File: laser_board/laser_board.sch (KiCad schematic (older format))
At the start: 14 parts

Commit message: Adding some goodies to the laser board: 1. Laser driver 2. AVR programmer 3. Fixing a wrong wiring (arduino pin #2) 4. Crystal oscillator 5. Reset pin
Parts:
- removed UL?: JohnsLaserDriver, symbol JohnsLaserDriver
- added C?: 100nF, symbol C
- added C? (x2): 22pF, symbol C
- added D? (x2): D, symbol D
- added LAIZAA: CONN_01X02, symbol CONN_01X02
- added PROG: CONN_02X03, symbol CONN_02X03
- added Q?: Q_NPN_EBC, symbol Q_NPN_EBC
- added R?: 10K, symbol R
- added R?: 1R0, symbol R
- added R?: 180R, symbol R
- added RV?: POT, symbol POT
- added U?: LM317T, TO-220, symbol LM317T
- added Y?: Crystal, symbol Crystal
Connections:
- wire segments 100 -> 171
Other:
- moved on the sheet: IC?

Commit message: Schematics changes: 1. Adding UART 2. Adding a power connector 3. Adding some footprints 4. Adding a reset button 5. Adding some decoupling capacitors
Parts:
- removed SW_MS1, SW_MS2, SW_MS3: SPST, symbol SPST
- added C?: 100nF, symbol C
- added C? (x3): 47uF, symbol CP
- added MICROSTEP: CONN_02X03, Pin_Headers:Pin_Header_Straight_2x03, symbol CONN_02X03
- added POWER: CONN_01X03, Sockets_MOLEX_KK-System:Socket_MOLEX-KK-RM2-54mm_Lock_3pin_straight, symbol CONN_01X03
- added R? (x2): 1K, symbol R
- added SW?: SW_PUSH, symbol SW_PUSH
- added UART: CONN_01X03, Pin_Headers:Pin_Header_Straight_1x03, symbol CONN_01X03
- LAIZAA, PSX, PSY: footprint (none) -> Sockets_MOLEX_KK-System:Socket_MOLEX-KK-RM2-54mm_Lock_2pin_straight
- PROG: footprint (none) -> Pin_Headers:Pin_Header_Straight_2x03
- PX1, PX2, PY: footprint (none) -> Sockets_MOLEX_KK-System:Socket_MOLEX-KK-RM2-54mm_Lock_4pin_straight
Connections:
- wire segments 171 -> 195
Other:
- moved on the sheet: D?, LAIZAA, R?, RV?, U?

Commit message: Adding a footprint for the A4988 board Assigning footprints Adding a PCB
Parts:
- removed C?: 100nF, symbol C
- removed Q?: Q_NPN_EBC, symbol Q_NPN_EBC
- added C4: 10uF, Capacitors_ThroughHole:C_Radial_D5_L11_P2.5, symbol CP
- added Q1: IRF540N, Power_Integrations:TO-220, symbol IRF540N
- added R6: 1R0, Resistors_ThroughHole:Resistor_Vertical_RM5mm, symbol R
- C1, C2, C3: renamed from C?; footprint (none) -> Capacitors_ThroughHole:C_Rect_L4_W2.5_P2.5
- C5, C6, C7: renamed from C?; footprint (none) -> Capacitors_ThroughHole:C_Radial_D6.3_L11.2_P2.5
- D1, D2: renamed from D?; footprint (none) -> Diodes_ThroughHole:Diode_DO-41_SOD81_Vertical_KathodeUp
- IC1: renamed from IC?; footprint DIL28 -> Housings_DIP:DIP-28_W7.62mm
- POWER1: renamed from POWER; symbol CONN_01X03 -> CONN_01X03-RESCUE-laser_board
- R1: value R -> 220R; footprint (none) -> Capacitors_ThroughHole:C_Rect_L4_W2.5_P2.5
- R2, R3, R4, R7: renamed from R?; footprint (none) -> Capacitors_ThroughHole:C_Rect_L4_W2.5_P2.5
- R5: renamed from R?; footprint (none) -> Resistors_ThroughHole:Resistor_Vertical_RM5mm
- RV1: renamed from RV?; footprint (none) -> Potentiometers:Potentiometer_Bourns_3006P_Angular_ScrewFront
- SW1: renamed from SW?; footprint (none) -> Pin_Headers:Pin_Header_Straight_1x02
- U1: renamed from U?; footprint TO-220 -> Power_Integrations:TO-220
- UART1: renamed from UART; symbol CONN_01X03 -> CONN_01X03-RESCUE-laser_board
- UX1, UX2: footprint (none) -> My_Shit:A4988
- UY1: renamed from UY; footprint (none) -> My_Shit:A4988
- Y1: renamed from Y?; footprint (none) -> Crystals:Crystal_HC49-U_Vertical
- renumbered LAIZAA to LAIZAA1, MICROSTEP to MICROSTEP1, PROG to PROG1, PSX to PSX1, PSY to PSY1, PY to PY1
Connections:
- wire segments 195 -> 158
- no-connect marks 0 -> 10
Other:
- moved on the sheet: R5, R7

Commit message: major PCB improvements
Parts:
- RV1: symbol POT -> POT-RESCUE-laser_board
- SW1: footprint Pin_Headers:Pin_Header_Straight_1x02 -> laser_footprints:SIMPLE_SWITCH
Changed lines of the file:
@@
 $EndComp
 $Comp
-L POT RV1
+L POT-RESCUE-laser_board RV1
 U 1 1 56D9FE62
 P 5150 6050
@@
 F 0 "SW1" H 4300 5060 50  0000 C CNN
 F 1 "SW_PUSH" H 4150 4870 50  0000 C CNN
-F 2 "Pin_Headers:Pin_Header_Straight_1x02" H 4150 4950 50  0001 C CNN
+F 2 "laser_footprints:SIMPLE_SWITCH" H 4150 4950 50  0001 C CNN
 F 3 "" H 4150 4950 50  0000 C CNN
 	1    4150 4950

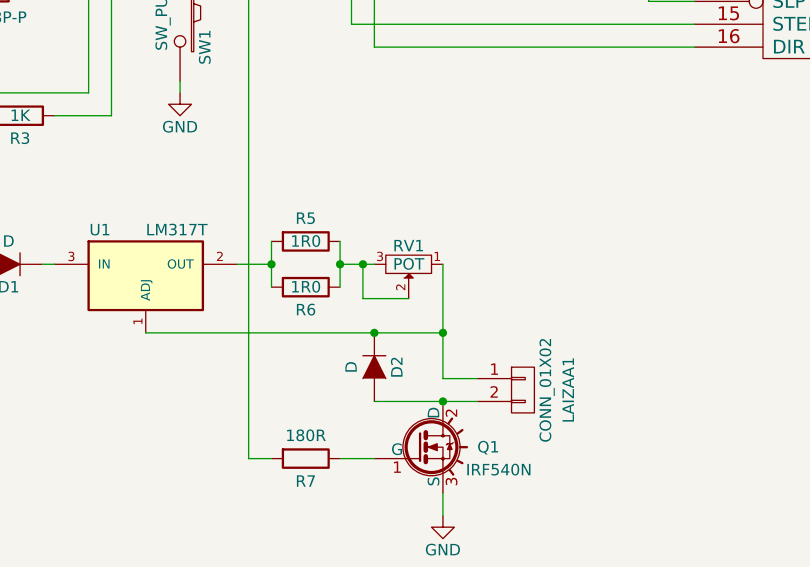
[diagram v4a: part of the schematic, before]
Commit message: fix a pot route in the laser board
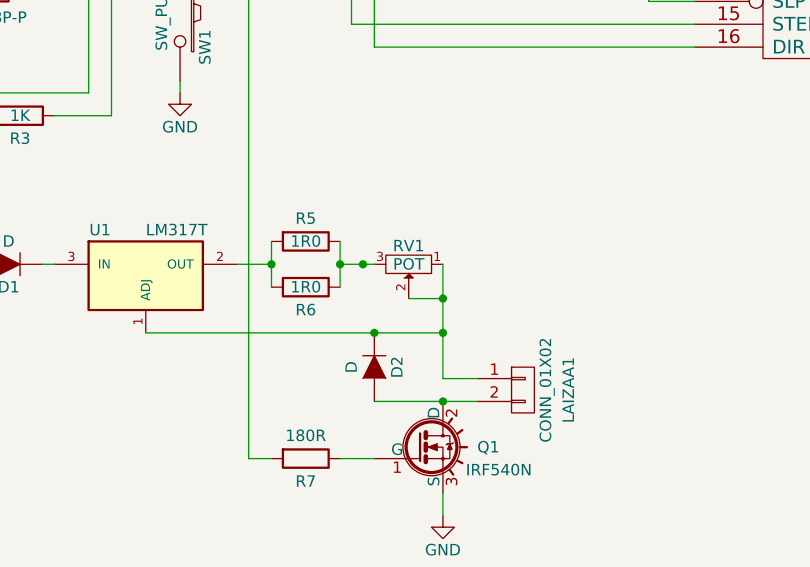
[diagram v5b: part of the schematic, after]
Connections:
- net at D2.1 (K), LAIZAA1.1 (P1), RV1.1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: now also RV1.2
- net at R5.1, R6.1, RV1.3: no longer RV1.2
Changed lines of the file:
@@
 	4850 6050 5000 6050
 Wire Wire Line
-	4950 6050 4950 6200
-Wire Wire Line
-	4950 6200 5150 6200
+	5300 6200 5150 6200
 Connection ~ 4950 6050
 Wire Wire Line
@@
 	1    0    0    -1
 $EndComp
+Connection ~ 5300 6200
 $EndSCHEMATC
